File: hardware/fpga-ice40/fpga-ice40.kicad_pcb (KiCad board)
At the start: 2 copper layers, 41 parts, among them J1 MicroSD_Molex_1040310811, J2 ProgHeader_iCE40, J3 ProgHeader_Flash_QSPI, U1 iCE40HX4K-TQ144, U2 IS42S16320F-6TL, U3 W25Q32JVZP, U4 W25Q32JVZP

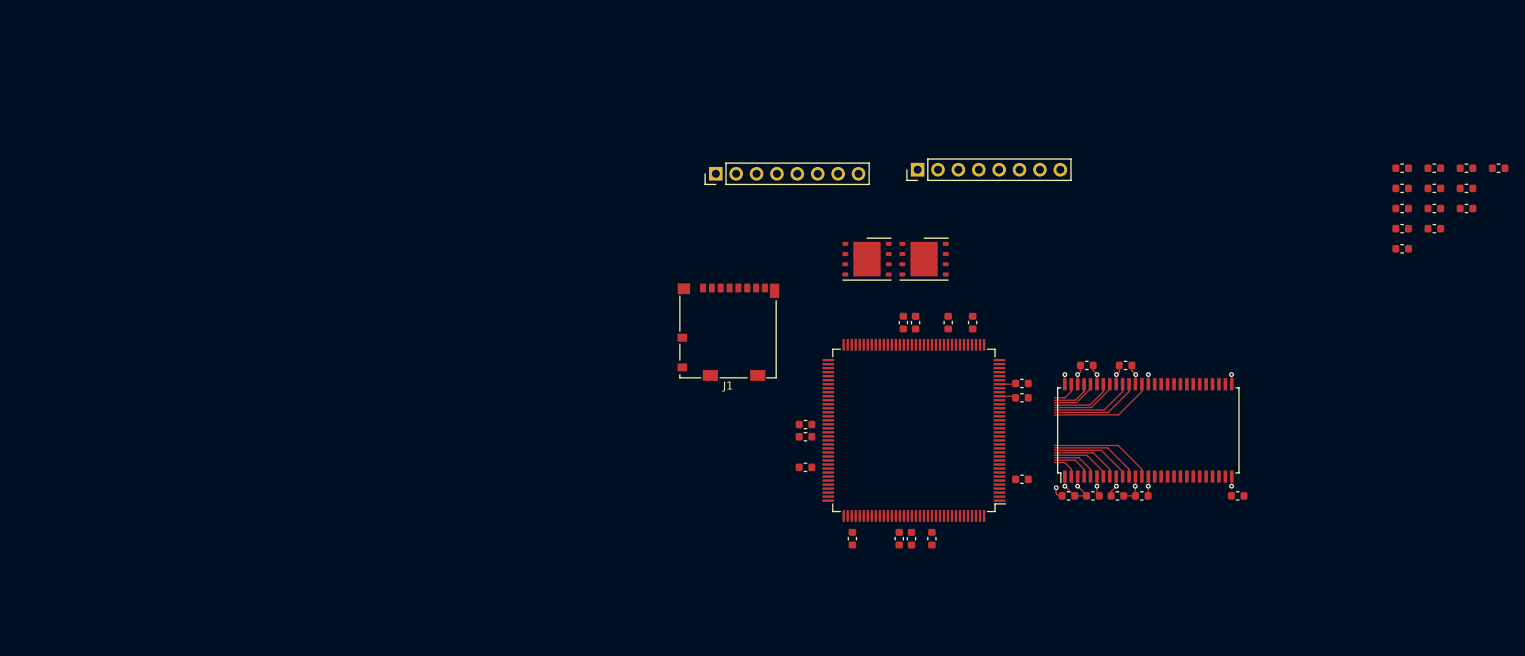
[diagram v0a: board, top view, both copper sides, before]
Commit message: Use a combined SOIC-8/16W layout for flash ICs
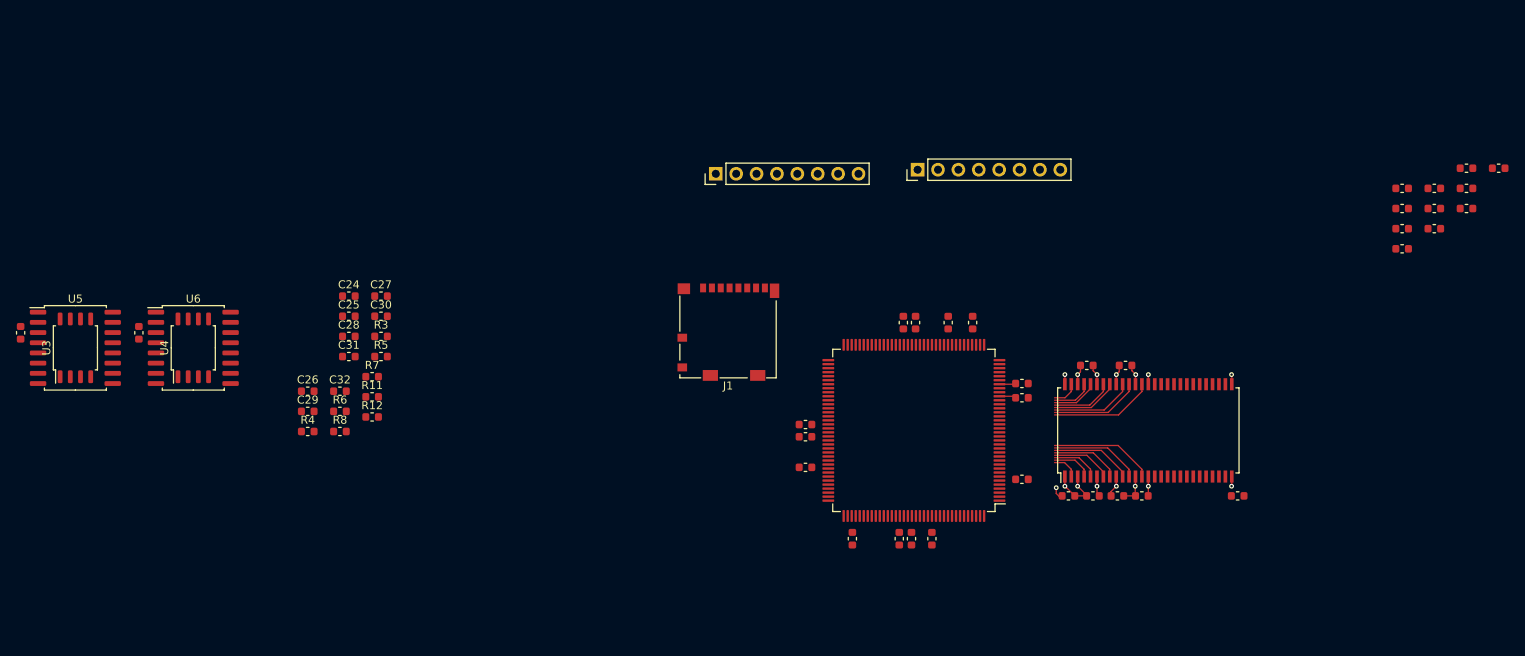
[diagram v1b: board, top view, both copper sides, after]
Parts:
- added C24: 100n, Capacitor_SMD:C_0603_1608Metric, F.Cu at (75.9, 84.9)
- added C25: 10u, Capacitor_SMD:C_0603_1608Metric, F.Cu at (75.9, 87.4)
- added C26: 100n, Capacitor_SMD:C_0603_1608Metric, F.Cu at (70.8, 96.7)
- added C27: 10u, Capacitor_SMD:C_0603_1608Metric, F.Cu at (79.9, 84.9)
- added C28: 10u, Capacitor_SMD:C_0603_1608Metric, F.Cu at (75.9, 89.9)
- added C29: 10u, Capacitor_SMD:C_0603_1608Metric, F.Cu at (70.8, 99.2)
- added C30: 10u, Capacitor_SMD:C_0603_1608Metric, F.Cu at (79.9, 87.4)
- added C31: 10u, Capacitor_SMD:C_0603_1608Metric, F.Cu at (75.9, 92.4)
- added C32: 1u, Capacitor_SMD:C_0603_1608Metric, F.Cu at (74.8, 96.7)
- added R11: 100R, Resistor_SMD:R_0603_1608Metric, F.Cu at (78.8, 97.4)
- added R12: 100R, Resistor_SMD:R_0603_1608Metric, F.Cu at (78.8, 99.9)
- added R3: 1R, Resistor_SMD:R_0603_1608Metric, F.Cu at (79.9, 89.9)
- added R4: 1R, Resistor_SMD:R_0603_1608Metric, F.Cu at (70.8, 101.7)
- added R5: 1R, Resistor_SMD:R_0603_1608Metric, F.Cu at (79.9, 92.4)
- added R6: 1R, Resistor_SMD:R_0603_1608Metric, F.Cu at (74.8, 99.2)
- added R7: 1R, Resistor_SMD:R_0603_1608Metric, F.Cu at (78.8, 94.9)
- added R8: 10k, Resistor_SMD:R_0603_1608Metric, F.Cu at (74.8, 101.7)
- added U5: S25FL256SAGMFI01, Package_SO:SOIC-16W_7.5x10.3mm_P1.27mm, F.Cu at (41.8, 91.3)
- added U6: S25FL256SAGMFI01, Package_SO:SOIC-16W_7.5x10.3mm_P1.27mm, F.Cu at (56.5, 91.3)
- C5: value 100n -> 10u
- U3, U4: value W25Q32JVZP -> W25Q32JVSS; footprint Package_SON:WSON-8-1EP_6x5mm_P1.27mm_EP3.4x4.3mm -> Package_SO:SOIC-8_5.275x5.275mm_P1.27mm
- moved C22 173.3 mm to (35.0, 89.4), turned to 270 degrees
- moved C23 162.7 mm to (49.7, 89.4), turned to 270 degrees
- moved U3 99.2 mm to (41.8, 91.3), turned to 90 degrees
- moved U4 91.7 mm to (56.5, 91.3), turned to 90 degrees
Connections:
- net +2V5 renamed VCC2V5
- C1 pad 1: +1V2 -> VCCINT
- C10 pad 1: +3V3 -> VCCIO1
- C11 pad 1: +3V3 -> VCCIO2
- C12 pad 1: +3V3 -> VCCIO2
- C13 pad 1: +3V3 -> VCCIO3
- C14 pad 1: +3V3 -> VCCIO3
- C15 pad 1: +3V3 -> P3V3_DRAM
- C16 pad 1: +3V3 -> P3V3_DRAM
- C17 pad 1: +3V3 -> P3V3_DRAM
- C18 pad 1: +3V3 -> P3V3_DRAM
- C19 pad 1: +3V3 -> P3V3_DRAM
- C2 pad 1: +1V2 -> VCCINT
- C20 pad 1: +3V3 -> P3V3_DRAM
- C21 pad 1: +3V3 -> P3V3_DRAM
- C22 pad 1: +3V3 -> P3V3_FLASH
- C23 pad 1: +3V3 -> P3V3_FLASH
- C3 pad 1: +1V2 -> VCCINT
- C4 pad 1: +1V2 -> VCCINT
- C5 pad 1: +1V2 -> VCCPLL0
- C5 pad 2: GND -> VCCGND0
- C6 pad 1: +1V2 -> VCCPLL0
- C6 pad 2: GND -> VCCGND0
- C7 pad 1: +3V3 -> VCCIO0
- C8 pad 1: +3V3 -> VCCIO0
- C9 pad 1: +3V3 -> VCCIO1
- J1 pad 4: +3V3 -> P3V3_SD
- J2 pad 1: +3V3 -> P3V3
- J3 pad 1: +3V3 -> P3V3
- R1 pad 1: +3V3 -> P3V3
- R2 pad 1: +3V3 -> P3V3
- U1 pad 100: +3V3 -> VCCIO1
- U1 pad 111: +1V2 -> VCCINT
- U1 pad 123: +3V3 -> VCCIO0
- U1 pad 126: +1V2 -> VCCPLL1
- U1 pad 127: GND -> VCCGND1
- U1 pad 131: +3V3 -> VCCIO0
- U1 pad 27: +1V2 -> VCCINT
- U1 pad 30: +3V3 -> VCCIO3
- U1 pad 40: +1V2 -> VCCINT
- U1 pad 46: +3V3 -> VCCIO2
- U1 pad 53: GND -> VCCGND0
- U1 pad 54: +1V2 -> VCCPLL0
- U1 pad 57: +3V3 -> VCCIO2
- U1 pad 6: +3V3 -> VCCIO3
- U1 pad 72: +3V3 -> VCCSPI
- U1 pad 89: +3V3 -> VCCIO1
- U1 pad 92: +1V2 -> VCCINT
- U2 pad 1: +3V3 -> P3V3_DRAM
- U2 pad 14: +3V3 -> P3V3_DRAM
- U2 pad 27: +3V3 -> P3V3_DRAM
- U2 pad 3: +3V3 -> P3V3_DRAM
- U2 pad 43: +3V3 -> P3V3_DRAM
- U2 pad 49: +3V3 -> P3V3_DRAM
- U2 pad 9: +3V3 -> P3V3_DRAM
- U3 pad 8: +3V3 -> P3V3_FLASH
- U4 pad 8: +3V3 -> P3V3_FLASH
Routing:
- net +3V3: track 20.8 -> 0.00 mm, vias 7 -> 0
- net P3V3_DRAM: track 0.00 -> 18.7 mm, vias 0 -> 7
- net VCCINT: track 0.00 -> 2.09 mm
- net +1V2: track 2.09 -> 0.00 mm
- net VCCIO3: track 0.00 -> 2.05 mm

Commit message: Begin pin assignments from FPGA to N64 bus and SDRAM
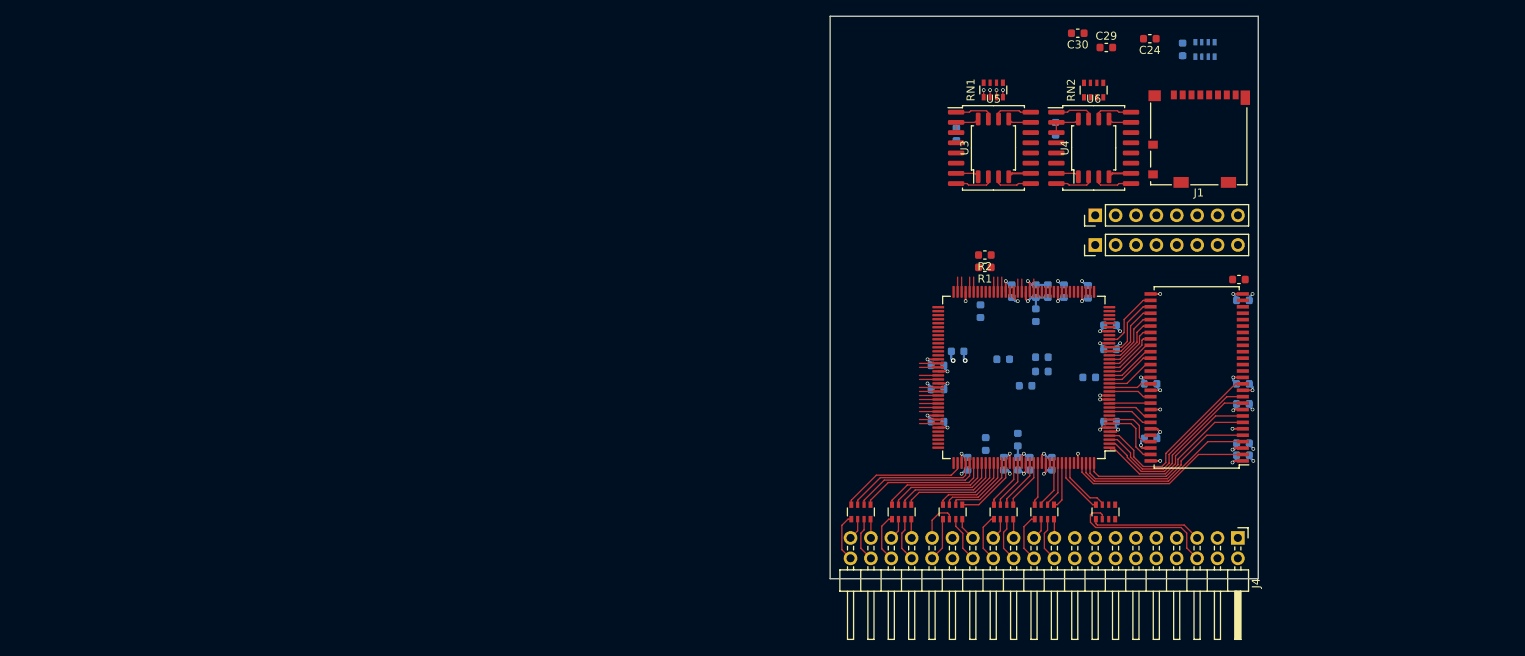
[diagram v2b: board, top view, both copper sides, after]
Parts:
- removed the C24 at (207.1, 71.4)
- removed R10, R9: 10k, Resistor_SMD:R_0603_1608Metric
- removed the R3 at (211.1, 74.0)
- removed the R4 at (207.1, 76.5)
- removed the R5 at (207.1, 79.0)
- removed the R6 at (215.2, 68.9)
- removed the R7 at (215.2, 71.4)
- removed the R8 at (211.1, 76.5)
- added J4: Conn_02x20_Odd_Even, Connector_PinHeader_2.54mm:PinHeader_2x20_P2.54mm_Horizontal, F.Cu at (186.7, 115.0)
- added RN1: 10k, Resistor_SMD:R_Array_Convex_4x0603, F.Cu at (156.2, 59.2)
- added RN2: 10k, Resistor_SMD:R_Array_Convex_4x0603, F.Cu at (168.7, 59.2)
- added RN3: 10k, Resistor_SMD:R_Array_Convex_4x0603, B.Cu at (182.6, 54.1)
- added RN4: 33R0, Resistor_SMD:R_Array_Convex_4x0603, F.Cu at (139.7, 111.8)
- added RN5: 33R0, Resistor_SMD:R_Array_Convex_4x0603, F.Cu at (144.8, 111.8)
- added RN6: 33R0, Resistor_SMD:R_Array_Convex_4x0603, F.Cu at (151.1, 111.8)
- added RN7: 33R0, Resistor_SMD:R_Array_Convex_4x0603, F.Cu at (157.5, 111.8)
- added RN8: 33R0, Resistor_SMD:R_Array_Convex_4x0603, F.Cu at (162.6, 111.8)
- added RN9: 33R0, Resistor_SMD:R_Array_Convex_4x0603, F.Cu at (170.2, 111.8)
- C1, C10, C11, C12, C13, C14, C15, C16, C17, C18, C19, C2, C20, C21, C22, C23, C25, C26, C27, C3, C31, C32, C4, C5, C6, C7, C8, C9, R11, R12, R3, R4, R5, R6, R7, R8: moved to B.Cu
- moved C22 119.2 mm to (151.6, 64.7)
- moved U3 117.1 mm to (156.2, 66.4)
- moved U5 117.1 mm to (156.2, 66.4)
- moved C23 117.0 mm to (164.0, 64.0)
- moved R8 115.3 mm to (179.8, 54.1), turned to 270 degrees
- moved U4 114.9 mm to (168.7, 66.4)
- moved U6 114.9 mm to (168.7, 66.4)
- moved C28 111.1 mm to (186.8, 82.8)
- moved C29 109.3 mm to (170.3, 53.9)
- moved C24 104.8 mm to (175.7, 52.8), turned to 180 degrees
- moved C30 93.7 mm to (166.7, 52.1), turned to 180 degrees
- moved R7 89.3 mm to (168.2, 95.0), turned to 180 degrees
- moved C26 88.9 mm to (159.2, 105.8), turned to 270 degrees
- moved C32 87.6 mm to (162.3, 92.5)
- moved C25 86.8 mm to (160.8, 105.8), turned to 270 degrees
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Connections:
- C27 pad 1: P3V3_DRAM -> P3V3_FPGA
- U1 pad 1: Net-(U1-Pad1) -> DRAM_DQ4
- U1 pad 10: Net-(U1-Pad10) -> DRAM_DQ12
- U1 pad 11: Net-(U1-Pad11) -> DRAM_DQ11
- U1 pad 110: Net-(U1-Pad110) -> N64_AD15_IC
- U1 pad 112: Net-(U1-Pad112) -> N64_AD0_IC
- U1 pad 113: Net-(U1-Pad113) -> N64_AD14_IC
- U1 pad 114: Net-(U1-Pad114) -> N64_AD1_IC
- U1 pad 115: Net-(U1-Pad115) -> N64_AD13_IC
- U1 pad 116: Net-(U1-Pad116) -> N64_AD2_IC
- U1 pad 117: Net-(U1-Pad117) -> N64_AD12_IC
- U1 pad 118: Net-(U1-Pad118) -> N64_AD3_IC
- U1 pad 119: Net-(U1-Pad119) -> N64_WRITEn_IC
- U1 pad 12: Net-(U1-Pad12) -> DRAM_DQ10
- U1 pad 120: Net-(U1-Pad120) -> N64_ALE_L_IC
- U1 pad 121: Net-(U1-Pad121) -> N64_READn_IC
- U1 pad 122: Net-(U1-Pad122) -> N64_ALE_H_IC
- U1 pad 124: Net-(U1-Pad124) -> N64_AD11_IC
- U1 pad 125: Net-(U1-Pad125) -> N64_AD4_IC
- U1 pad 128: Net-(U1-Pad128) -> N64_AD10_IC
- U1 pad 129: Net-(U1-Pad129) -> N64_AD5_IC
- U1 pad 130: Net-(U1-Pad130) -> N64_AD9_IC
- U1 pad 134: Net-(U1-Pad134) -> N64_AD6_IC
- U1 pad 135: Net-(U1-Pad135) -> N64_AD8_IC
- U1 pad 136: Net-(U1-Pad136) -> N64_AD7_IC
- U1 pad 137: Net-(U1-Pad137) -> N64_COLD_RESETn_IC
- U1 pad 138: Net-(U1-Pad138) -> N64_OS_EVENTn_IC
- U1 pad 141: Net-(U1-Pad141) -> DRAM_DQ0
- U1 pad 142: Net-(U1-Pad142) -> DRAM_DQ1
- U1 pad 143: Net-(U1-Pad143) -> DRAM_DQ2
- U1 pad 144: Net-(U1-Pad144) -> DRAM_DQ3
- U1 pad 15: Net-(U1-Pad15) -> DRAM_DQ9
- U1 pad 16: Net-(U1-Pad16) -> DRAM_DQ8
- U1 pad 17: Net-(U1-Pad17) -> DRAM_UDQM
- U1 pad 18: Net-(U1-Pad18) -> DRAM_CLK
- U1 pad 19: Net-(U1-Pad19) -> DRAM_CKE
- U1 pad 2: Net-(U1-Pad2) -> DRAM_DQ5
- U1 pad 20: Net-(U1-Pad20) -> DRAM_A12
- U1 pad 21: Net-(U1-Pad21) -> DRAM_A11
- U1 pad 22: Net-(U1-Pad22) -> DRAM_A9
- U1 pad 23: Net-(U1-Pad23) -> DRAM_A8
- U1 pad 24: Net-(U1-Pad24) -> DRAM_A7
- U1 pad 25: Net-(U1-Pad25) -> DRAM_A6
- U1 pad 26: Net-(U1-Pad26) -> DRAM_A5
- U1 pad 28: Net-(U1-Pad28) -> DRAM_A4
- U1 pad 3: Net-(U1-Pad3) -> DRAM_DQ6
- U1 pad 4: Net-(U1-Pad4) -> DRAM_DQ7
- U1 pad 47: FLASH_SSn -> Net-(U1-Pad47)
- U1 pad 48: FLASH_SCK -> FLASH_SSn
- U1 pad 49: Net-(U1-Pad49) -> FLASH_SCK
- U1 pad 7: Net-(U1-Pad7) -> DRAM_DQ15
- U1 pad 8: Net-(U1-Pad8) -> DRAM_DQ14
- U1 pad 9: Net-(U1-Pad9) -> DRAM_DQ13
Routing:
- net GND: track 16.6 -> 44.2 mm, vias 8 -> 27
- net DRAM_DQ0: track 3.33 -> 23.3 mm
- net N64_OS_EVENTn: track 0.00 -> 19.4 mm
- net DRAM_DQ1: track 5.06 -> 23.2 mm
- net DRAM_DQ2: track 5.99 -> 23.2 mm
- net N64_AD0_IC: track 0.00 -> 16.8 mm
- net N64_AD14_IC: track 0.00 -> 16.6 mm
- net N64_AD1_IC: track 0.00 -> 16.4 mm
- net N64_AD15_IC: track 0.00 -> 16.2 mm
- net DRAM_DQ3: track 7.53 -> 23.0 mm
- net N64_AD13_IC: track 0.00 -> 14.2 mm
- net N64_AD2_IC: track 0.00 -> 13.9 mm
- net N64_COLD_RESETn: track 0.00 -> 13.9 mm
- net N64_AD12_IC: track 0.00 -> 13.6 mm
- net N64_AD3_IC: track 0.00 -> 13.3 mm
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- added copper zone on In2(PWR).Cu, net P1V2
- added copper zone on In2(PWR).Cu, net P3V3_FPGA
- added copper zone on In2(PWR).Cu, net VCCIO0
- added copper zone on In2(PWR).Cu, net VCCIO1
- added copper zone on In2(PWR).Cu, net VCCIO2
- added copper zone on In2(PWR).Cu, net VCCIO3
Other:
- board outline added: 53.3 x 70.1 mm
- copper layers 2 -> 4
- net class FPGA_VCC added: clearance 0.1524, trace_width 0.254, via_dia 0.45, via_drill 0.3
- net class GND added: clearance 0.1524, trace_width 0.254, via_dia 0.6, via_drill 0.3
- rule via_min_drill: 0.3 -> 0.2
- rule via_min_size: 0.6 -> 0.45
